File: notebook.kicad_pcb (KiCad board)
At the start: 2 copper layers, 130 x 180 mm, 234 parts, among them J1 SWD, J2 BOOT, J3 ConnA, J4 ConnB, Q1 IRF7403, Q2 IRF7403, Q3 IRF7403, Q4 IRF7403, Q5 IRF7403, Q6 IRF7403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

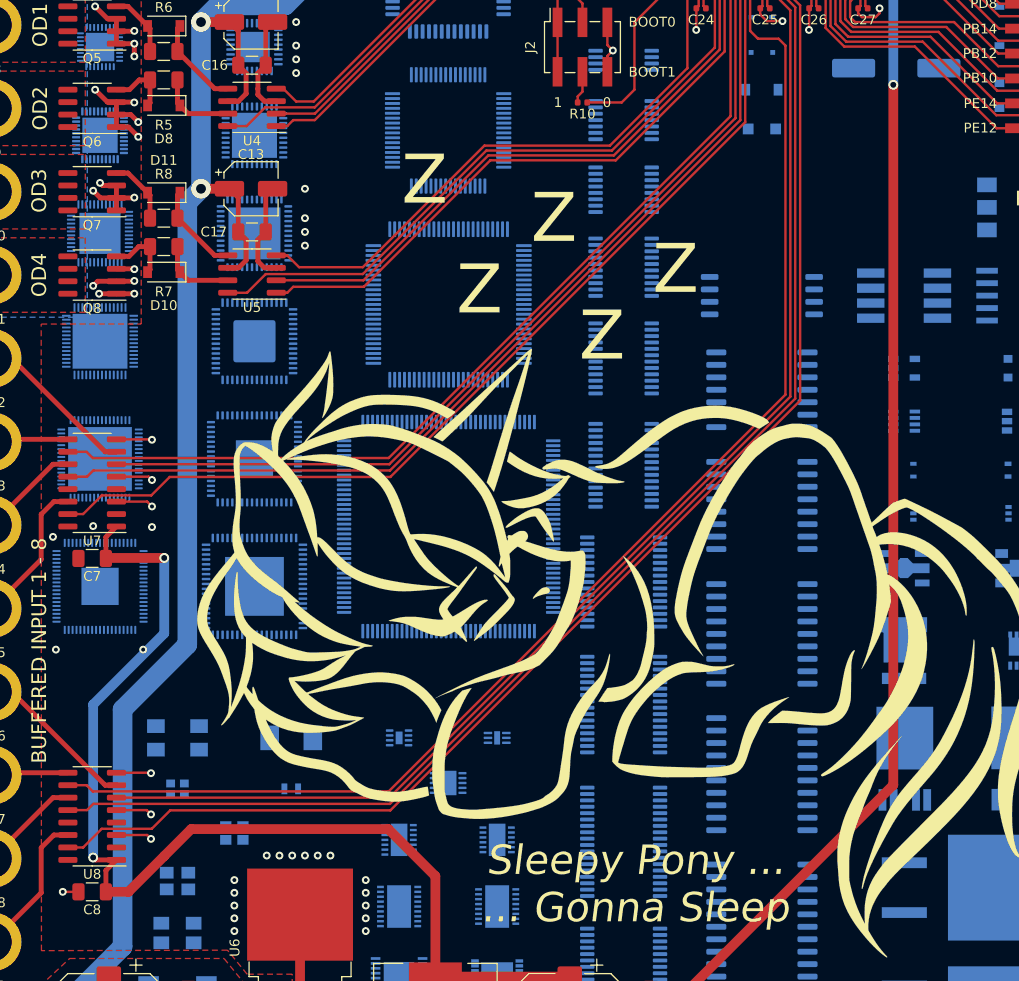
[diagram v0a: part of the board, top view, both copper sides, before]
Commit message: Add OSHWA mark
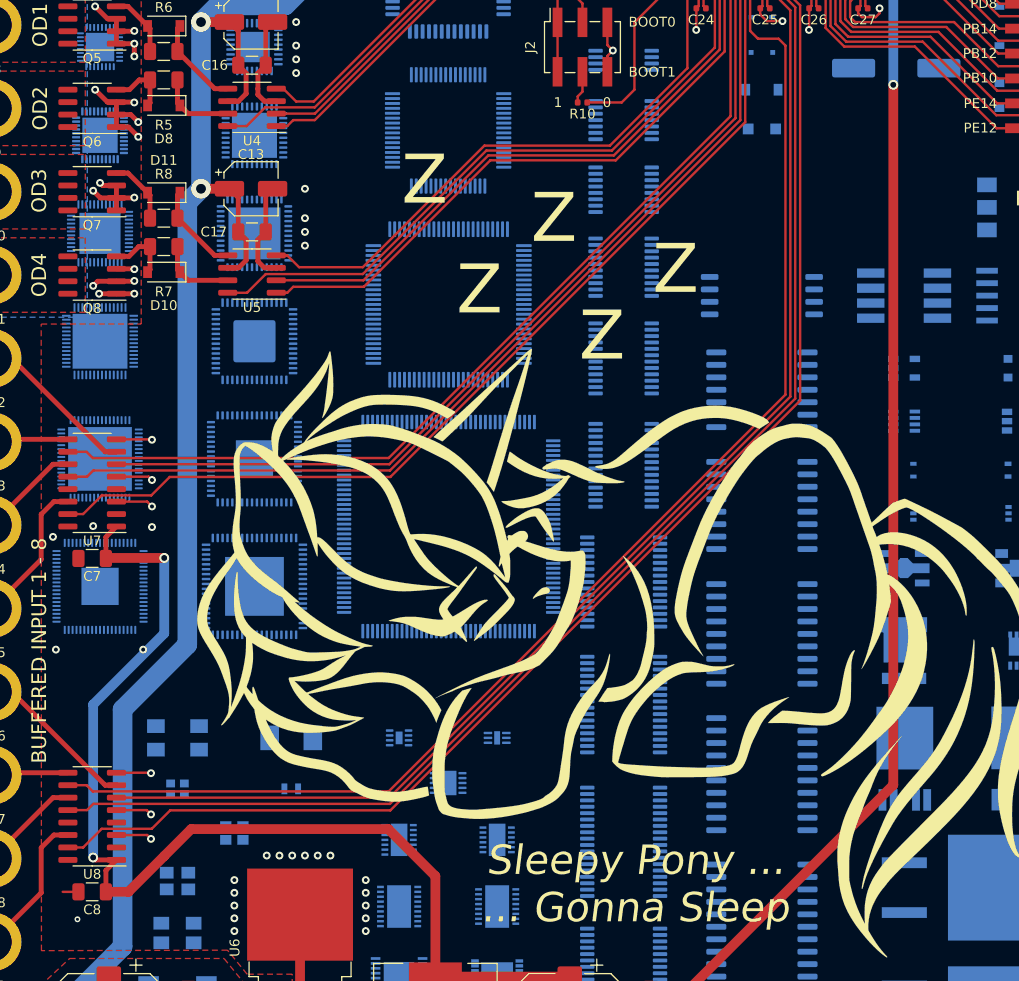
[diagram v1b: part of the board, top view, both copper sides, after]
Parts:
- added REF**: OSHW-Symbol_8.9x8mm_SilkScreen, Symbol:OSHW-Symbol_8.9x8mm_SilkScreen, B.Cu at (54.1, 187.2)
- added Ref**: Val**, notebook:TH000006_svg2sz, B.Cu at (54.5, 174.2)

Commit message: WIP schematics
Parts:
- removed the QFN20 at (56.0, 74.2)
- removed the QFN24 at (56.0, 81.8)
- removed the QFN28 at (56.0, 89.8)
- removed the QFN32 at (56.0, 98.2)
- removed QFN40: QFN-40-1EP_5x5mm_P0.4mm_EP3.6x3.6mm, Package_DFN_QFN:QFN-40-1EP_5x5mm_P0.4mm_EP3.6x3.6mm
- removed the QFN48 at (56.0, 117.2)
- removed the QFN56 at (56.0, 128.2)
- removed the QFN64 at (56.0, 140.2)
- removed QFN76: QFN-76-1EP_9x9mm_P0.4mm_EP3.8x3.8mm, Package_DFN_QFN:QFN-76-1EP_9x9mm_P0.4mm_EP3.8x3.8mm
- added REF**: CP_EIA-7361-38_AVX-V, Capacitor_Tantalum_SMD:CP_EIA-7361-38_AVX-V, B.Cu at (-6.60, 95.5)
- added REF**: CP_EIA-7343-15_Kemet-W, Capacitor_Tantalum_SMD:CP_EIA-7343-15_Kemet-W, B.Cu at (-6.60, 88.4)
- added REF**: CP_EIA-6032-15_Kemet-U, Capacitor_Tantalum_SMD:CP_EIA-6032-15_Kemet-U, B.Cu at (-6.60, 82.7)
- added REF**: CP_EIA-3528-12_Kemet-T, Capacitor_Tantalum_SMD:CP_EIA-3528-12_Kemet-T, B.Cu at (-6.60, 77.7)
- added REF**: CP_EIA-3216-10_Kemet-I, Capacitor_Tantalum_SMD:CP_EIA-3216-10_Kemet-I, B.Cu at (-6.60, 73.7)
- added REF**: CP_EIA-2012-12_Kemet-R, Capacitor_Tantalum_SMD:CP_EIA-2012-12_Kemet-R, B.Cu at (-6.60, 70.4)
- added REF**: CP_EIA-1608-08_AVX-J, Capacitor_Tantalum_SMD:CP_EIA-1608-08_AVX-J, B.Cu at (-6.60, 67.3)
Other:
- board text added: "DFN 0.5mm"
- board text removed: "QFN 0.4mm"
